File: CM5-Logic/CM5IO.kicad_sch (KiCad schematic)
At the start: 11 parts, among them J12 39291247, J2 B2B-PH-K-S, J20 ED555/4DS, J3 B2B-PH-K-S, J4 39291087, J6 691210910006, J7 691210910006

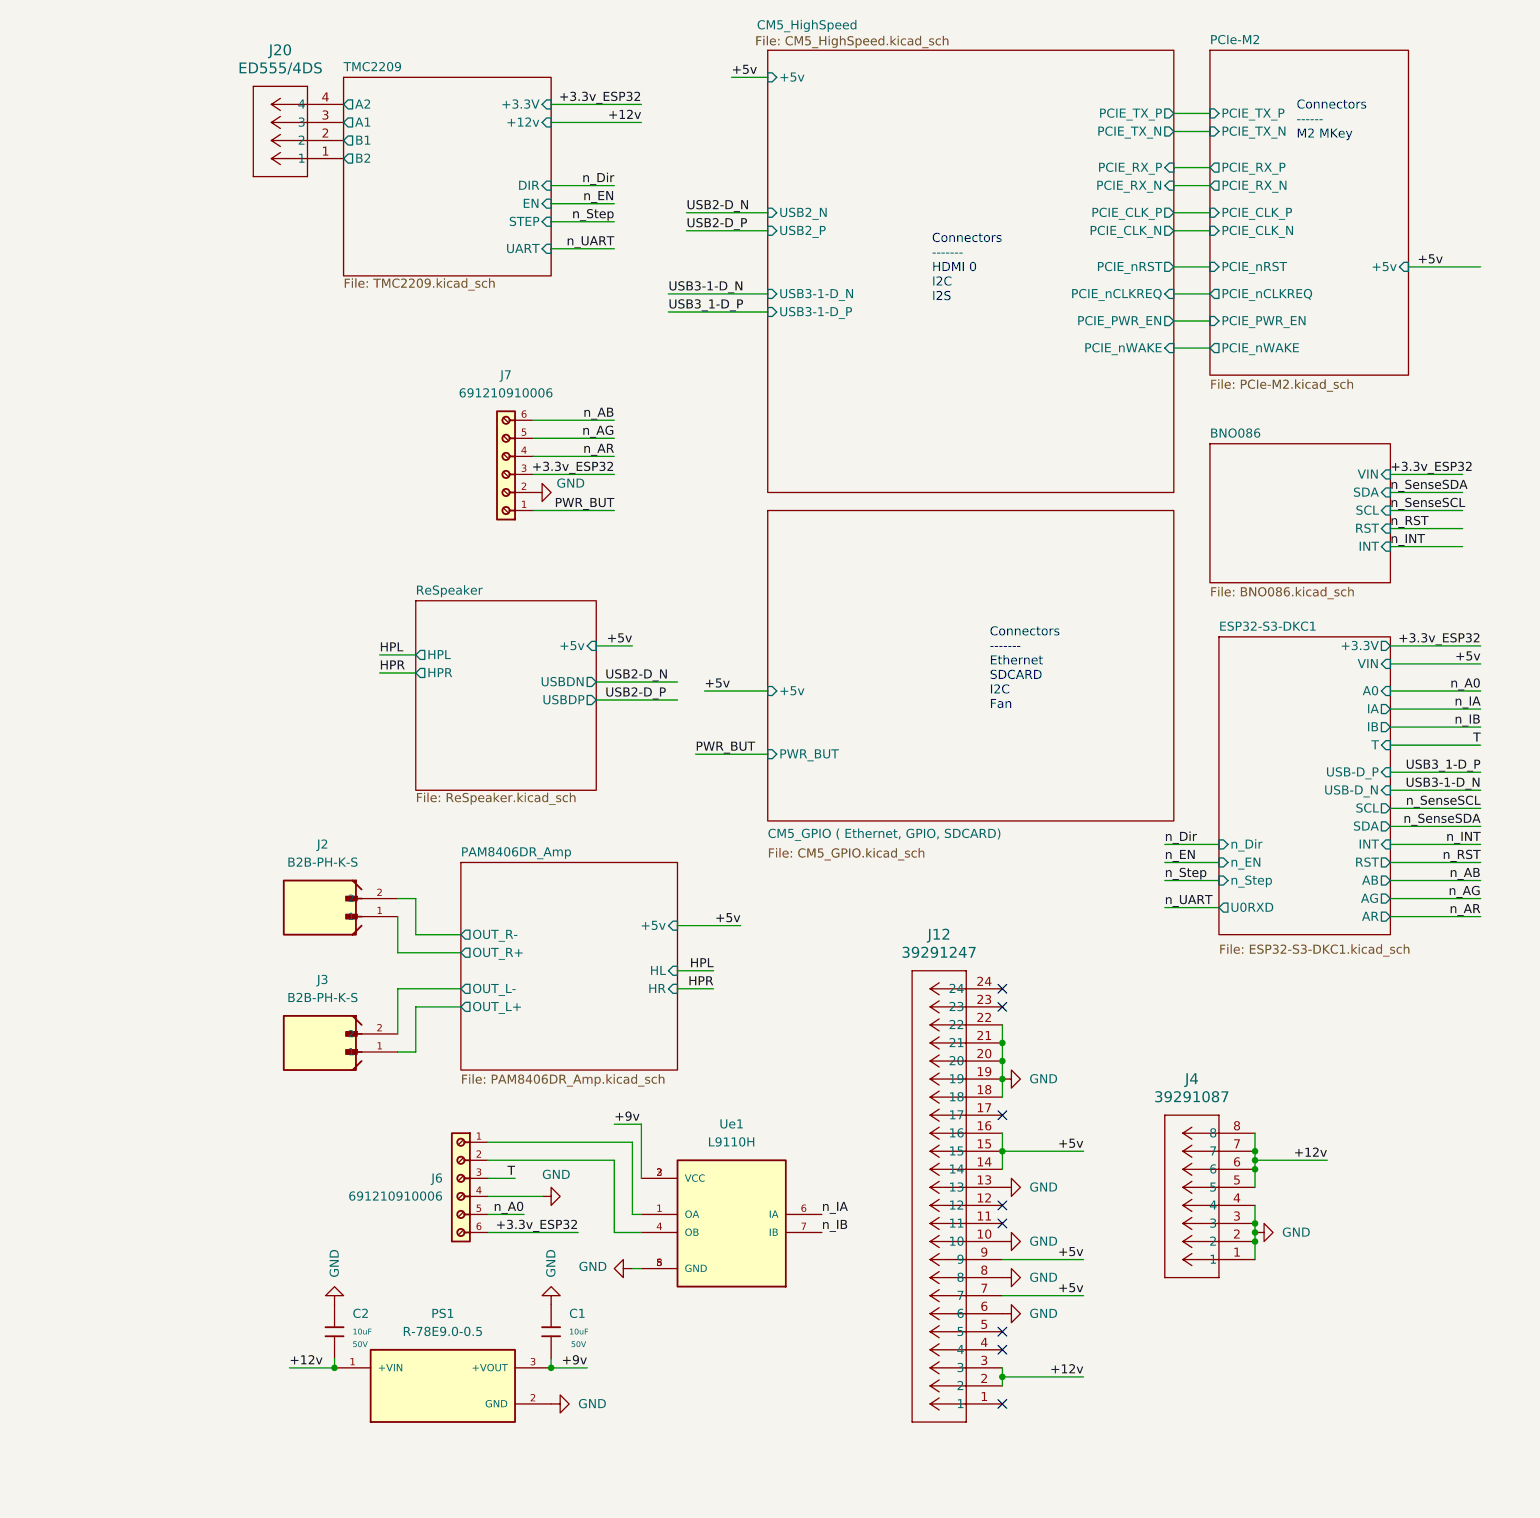
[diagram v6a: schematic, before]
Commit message: changes USB port, adds TMC2209 SilentStepStick footprint, redoes PCB Layout
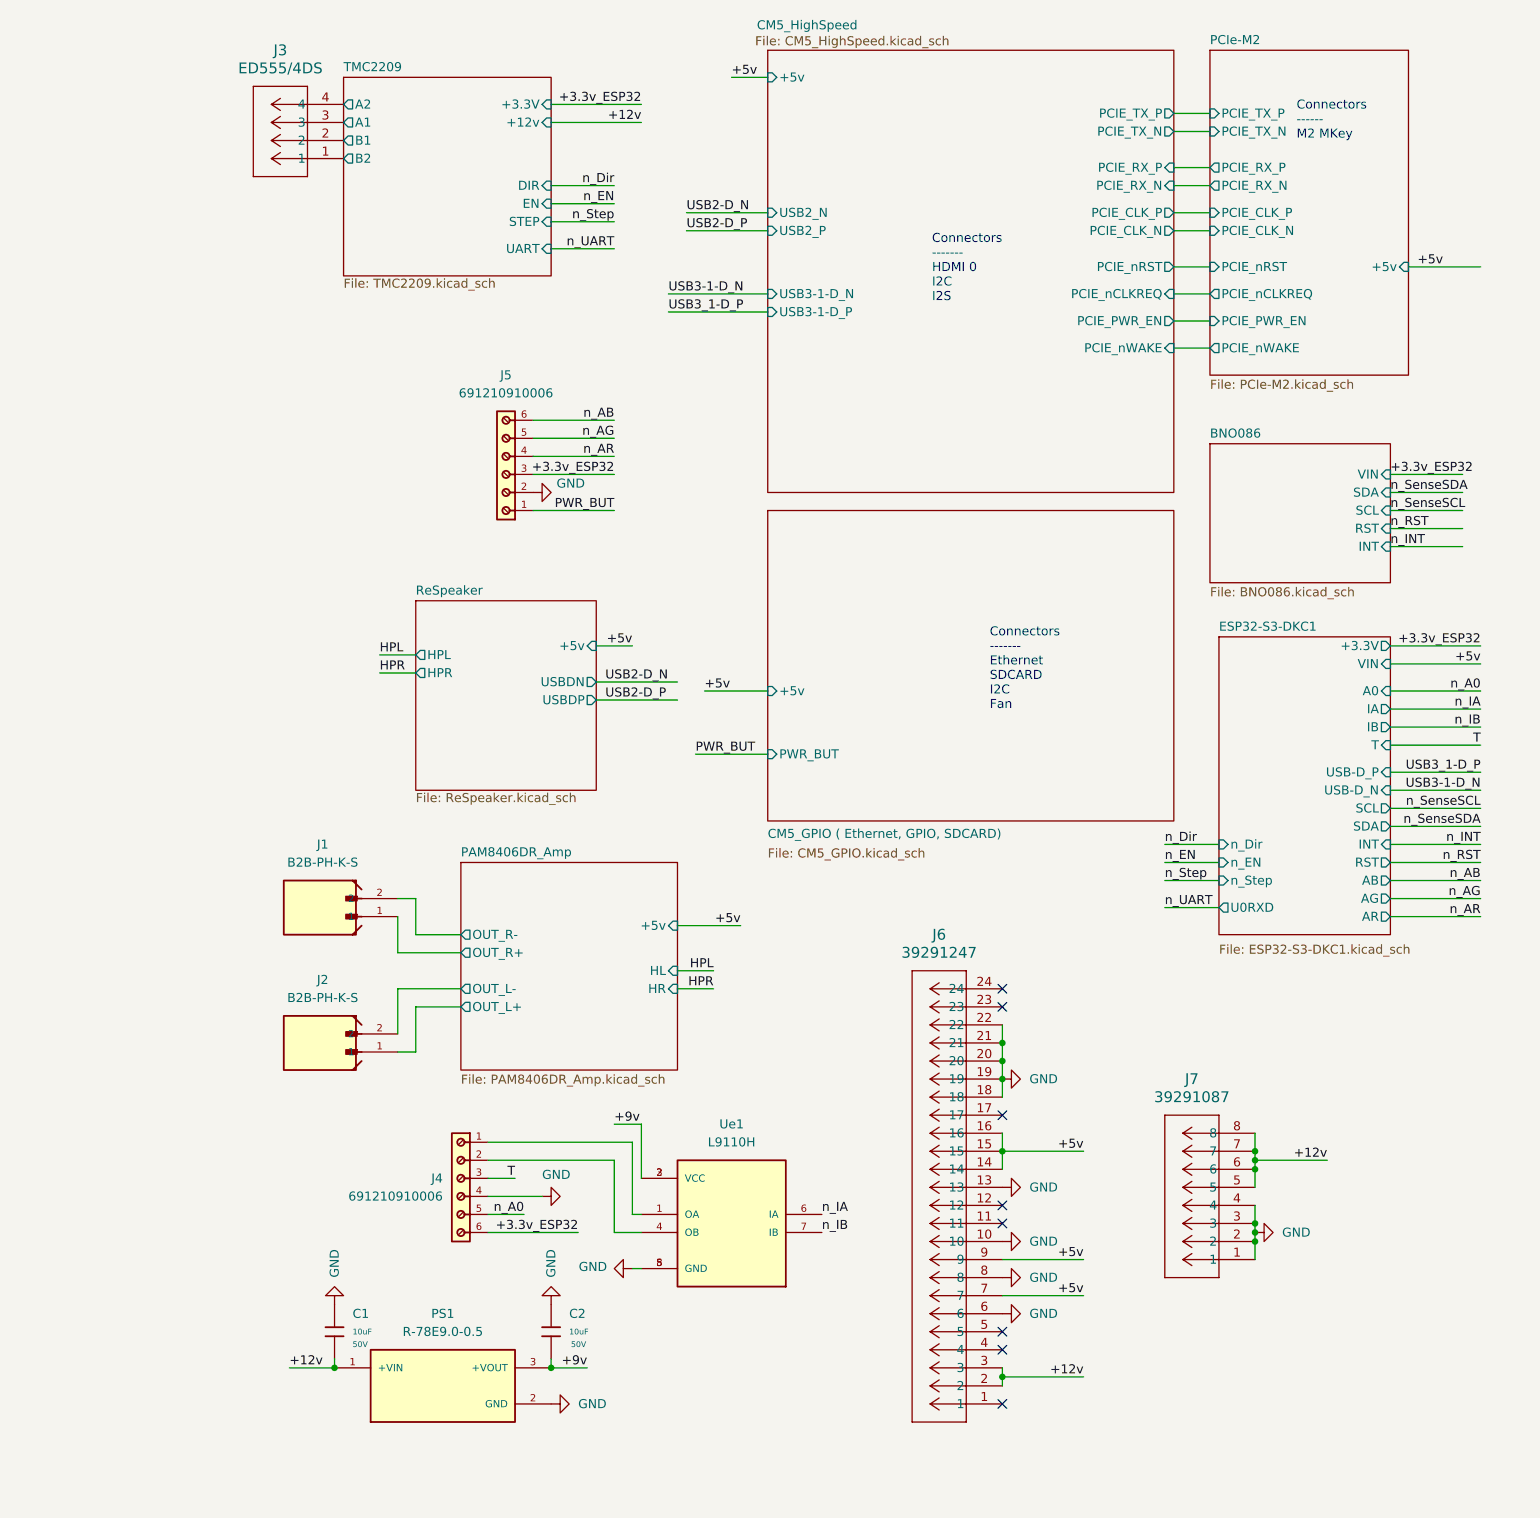
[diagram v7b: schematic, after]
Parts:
- PS1: footprint R-78E9.0-0.5:CONV_R-78E9.0-0.5 -> Custom Components:CONV_R-78E9.0-0.5
- renumbered C2 to C1, C1 to C2, J2 to J1, J3 to J2, J20 to J3, J6 to J4, J7 to J5, J12 to J6, J4 to J7
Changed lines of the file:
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@@
 		(dnp no)
 		(fields_autoplaced yes)
-		(property "Reference" "J4"
+		(property "Reference" "J7"
 			(at 509.27 179.07 0)
 			(effects
@@
 			(project ""
 				(path "/e63e39d7-6ac0-4ffd-8aa3-1841a4541b55"
-					(reference "J4")
+					(reference "J7")
 					(unit 1)
 				)
@@
 		(dnp no)
 		(fields_autoplaced yes)
-		(property "Reference" "#PWR074"
+		(property "Reference" "#PWR012"
 			(at 524.51 200.66 0)
 			(effects
@@
 			(project "CM5IO"
 				(path "/e63e39d7-6ac0-4ffd-8aa3-1841a4541b55"
-					(reference "#PWR074")
+					(reference "#PWR012")
 					(unit 1)
 				)
@@
 		(dnp no)
 		(fields_autoplaced yes)
-		(property "Reference" "J2"
+		(property "Reference" "J1"
 			(at 386.9531 146.05 0)
 			(effects
@@
 			(project "CM5IO"
 				(path "/e63e39d7-6ac0-4ffd-8aa3-1841a4541b55"
-					(reference "J2")
+					(reference "J1")
 					(unit 1)
 				)
@@
 		(on_board yes)
 		(dnp no)
-		(property "Reference" "#PWR06"
+		(property "Reference" "#PWR03"
 			(at 424.18 195.58 0)
 			(effects
@@
 			(project "CM5IO"
 				(path "/e63e39d7-6ac0-4ffd-8aa3-1841a4541b55"
-					(reference "#PWR06")
+					(reference "#PWR03")
 					(unit 1)
 				)
@@
 		(on_board yes)
 		(dnp no)
-		(property "Reference" "#PWR01"
+		(property "Reference" "#PWR04"
 			(at 419.1 204.47 0)
 			(effects
@@
 			(project "CM5IO"
 				(path "/e63e39d7-6ac0-4ffd-8aa3-1841a4541b55"
-					(reference "#PWR01")
+					(reference "#PWR04")
 					(unit 1)
 				)
@@
 		(dnp no)
 		(fields_autoplaced yes)
-		(property "Reference" "#PWR066"
+		(property "Reference" "#PWR08"
 			(at 488.95 194.31 0)
 			(effects
@@
 			(project ""
 				(path "/e63e39d7-6ac0-4ffd-8aa3-1841a4541b55"
-					(reference "#PWR066")
+					(reference "#PWR08")
 					(unit 1)
 				)
@@
 		(dnp no)
 		(fields_autoplaced yes)
-		(property "Reference" "#PWR073"
+		(property "Reference" "#PWR09"
 			(at 488.95 201.93 0)
 			(effects
@@
 			(project "CM5IO"
 				(path "/e63e39d7-6ac0-4ffd-8aa3-1841a4541b55"
-					(reference "#PWR073")
+					(reference "#PWR09")
 					(unit 1)
 				)
@@
 		(dnp no)
 		(fields_autoplaced yes)
-		(property "Reference" "#PWR072"
+		(property "Reference" "#PWR010"
 			(at 488.95 207.01 0)
 			(effects
@@
 			(project "CM5IO"
 				(path "/e63e39d7-6ac0-4ffd-8aa3-1841a4541b55"
-					(reference "#PWR072")
+					(reference "#PWR010")
 					(unit 1)
 				)
@@
 		(dnp no)
 		(fields_autoplaced yes)
-		(property "Reference" "J7"
+		(property "Reference" "J5"
 			(at 412.75 80.01 90)
 			(effects
@@
 			(project ""
 				(path "/e63e39d7-6ac0-4ffd-8aa3-1841a4541b55"
-					(reference "J7")
+					(reference "J5")
 					(unit 1)
 				)
@@
 		(dnp no)
 		(fields_autoplaced yes)
-		(property "Reference" "#PWR067"
+		(property "Reference" "#PWR07"
 			(at 488.95 179.07 0)
 			(effects
@@
 			(project "CM5IO"
 				(path "/e63e39d7-6ac0-4ffd-8aa3-1841a4541b55"
-					(reference "#PWR067")
+					(reference "#PWR07")
 					(unit 1)
 				)
@@
 		(dnp no)
 		(fields_autoplaced yes)
-		(property "Reference" "J3"
+		(property "Reference" "J2"
 			(at 386.9531 165.1 0)
 			(effects
@@
 			(project "CM5IO"
 				(path "/e63e39d7-6ac0-4ffd-8aa3-1841a4541b55"
-					(reference "J3")
+					(reference "J2")
 					(unit 1)
 				)
@@
 		(on_board yes)
 		(dnp no)
-		(property "Reference" "#PWR08"
+		(property "Reference" "#PWR02"
 			(at 422.91 96.52 0)
 			(effects
@@
 			(project ""
 				(path "/e63e39d7-6ac0-4ffd-8aa3-1841a4541b55"
-					(reference "#PWR08")
+					(reference "#PWR02")
 					(unit 1)
 				)
@@
 		(on_board yes)
 		(dnp no)
-		(property "Reference" "C1"
+		(property "Reference" "C2"
 			(at 421.64 212.0899 0)
 			(effects
@@
 			(project "CM5IO"
 				(path "/e63e39d7-6ac0-4ffd-8aa3-1841a4541b55"
-					(reference "C1")
+					(reference "C2")
 					(unit 1)
 				)
@@
 		(dnp no)
 		(fields_autoplaced yes)
-		(property "Reference" "J6"
+		(property "Reference" "J4"
 			(at 403.86 193.0399 90)
 			(effects
@@
 			(project ""
 				(path "/e63e39d7-6ac0-4ffd-8aa3-1841a4541b55"
-					(reference "J6")
+					(reference "J4")
 					(unit 1)
 				)
@@
 		(dnp no)
 		(fields_autoplaced yes)
-		(property "Reference" "J20"
+		(property "Reference" "J3"
 			(at 381 34.29 0)
 			(effects
@@
 			(project ""
 				(path "/e63e39d7-6ac0-4ffd-8aa3-1841a4541b55"
-					(reference "J20")
+					(reference "J3")
 					(unit 1)
 				)
@@
 		(on_board yes)
 		(dnp no)
-		(property "Reference" "#PWR04"
+		(property "Reference" "#PWR06"
 			(at 424.18 205.74 0)
 			(effects
@@
 			(project "CM5IO"
 				(path "/e63e39d7-6ac0-4ffd-8aa3-1841a4541b55"
-					(reference "#PWR04")
+					(reference "#PWR06")
 					(unit 1)
 				)
@@
 		(dnp no)
 		(fields_autoplaced yes)
-		(property "Reference" "J12"
+		(property "Reference" "J6"
 			(at 473.71 158.75 0)
 			(effects
@@
 			(project ""
 				(path "/e63e39d7-6ac0-4ffd-8aa3-1841a4541b55"
-					(reference "J12")
+					(reference "J6")
 					(unit 1)
 				)
@@
 		(on_board yes)
 		(dnp no)
-		(property "Reference" "#PWR02"
+		(property "Reference" "#PWR01"
 			(at 388.62 204.47 0)
 			(effects
@@
 			(project "CM5IO"
 				(path "/e63e39d7-6ac0-4ffd-8aa3-1841a4541b55"
-					(reference "#PWR02")
+					(reference "#PWR01")
 					(unit 1)
 				)
@@
 		(on_board yes)
 		(dnp no)
-		(property "Reference" "#PWR03"
+		(property "Reference" "#PWR05"
 			(at 425.45 224.79 0)
 			(effects
@@
 			(project "CM5IO"
 				(path "/e63e39d7-6ac0-4ffd-8aa3-1841a4541b55"
-					(reference "#PWR03")
+					(reference "#PWR05")
 					(unit 1)
 				)
@@
 			)
 		)
-		(property "Footprint" "R-78E9.0-0.5:CONV_R-78E9.0-0.5"
+		(property "Footprint" "Custom Components:CONV_R-78E9.0-0.5"
 			(at 403.86 222.25 0)
 			(effects
@@
 		(dnp no)
 		(fields_autoplaced yes)
-		(property "Reference" "#PWR069"
+		(property "Reference" "#PWR011"
 			(at 488.95 212.09 0)
 			(effects
@@
 			(project "CM5IO"
 				(path "/e63e39d7-6ac0-4ffd-8aa3-1841a4541b55"
-					(reference "#PWR069")
+					(reference "#PWR011")
 					(unit 1)
 				)
@@
 		(on_board yes)
 		(dnp no)
-		(property "Reference" "C2"
+		(property "Reference" "C1"
 			(at 391.16 212.0899 0)
 			(effects
@@
 			(project "CM5IO"
 				(path "/e63e39d7-6ac0-4ffd-8aa3-1841a4541b55"
-					(reference "C2")
-					(unit 1)
-				)
+					(reference "C1")
+					(unit 1)
+				)

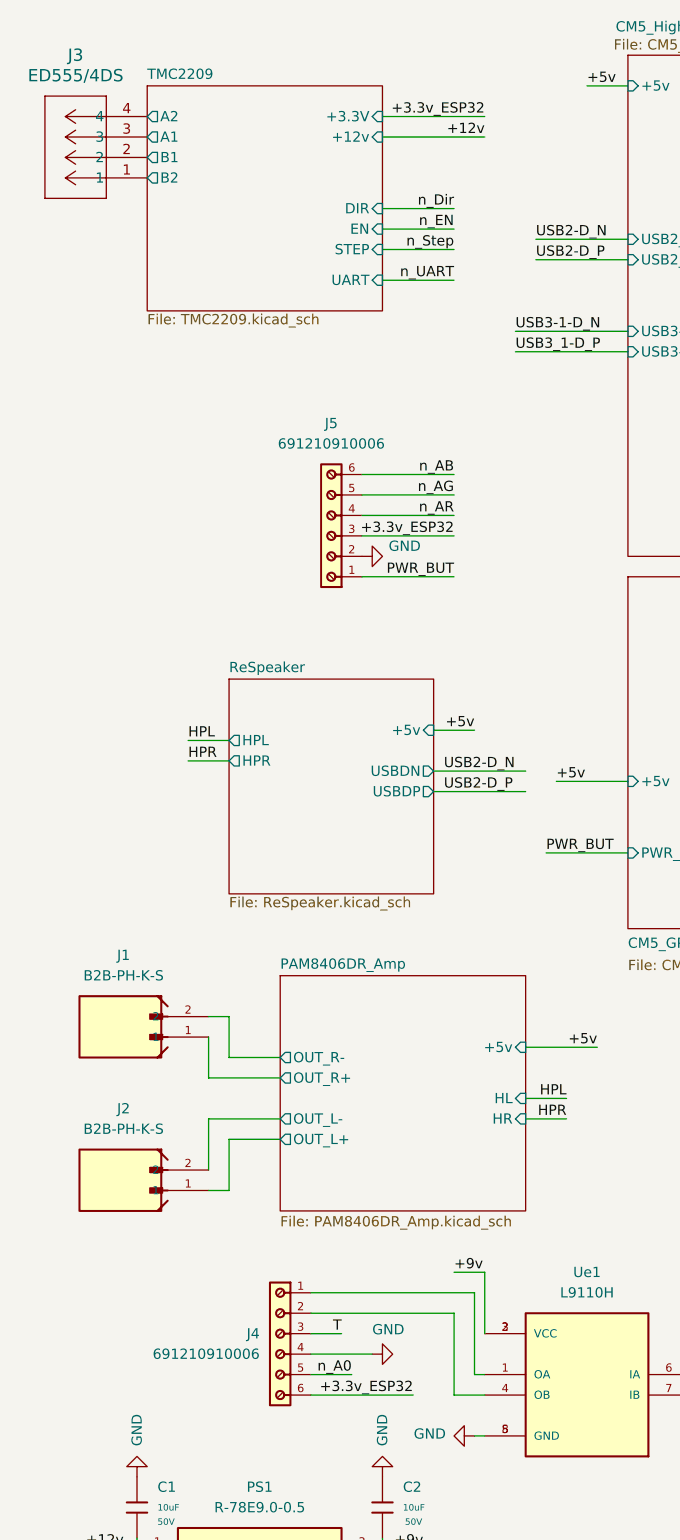
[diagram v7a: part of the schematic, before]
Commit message: Finishes PCB Pad Layout, Updates LED Status Circuit to RPI Foundations newest version
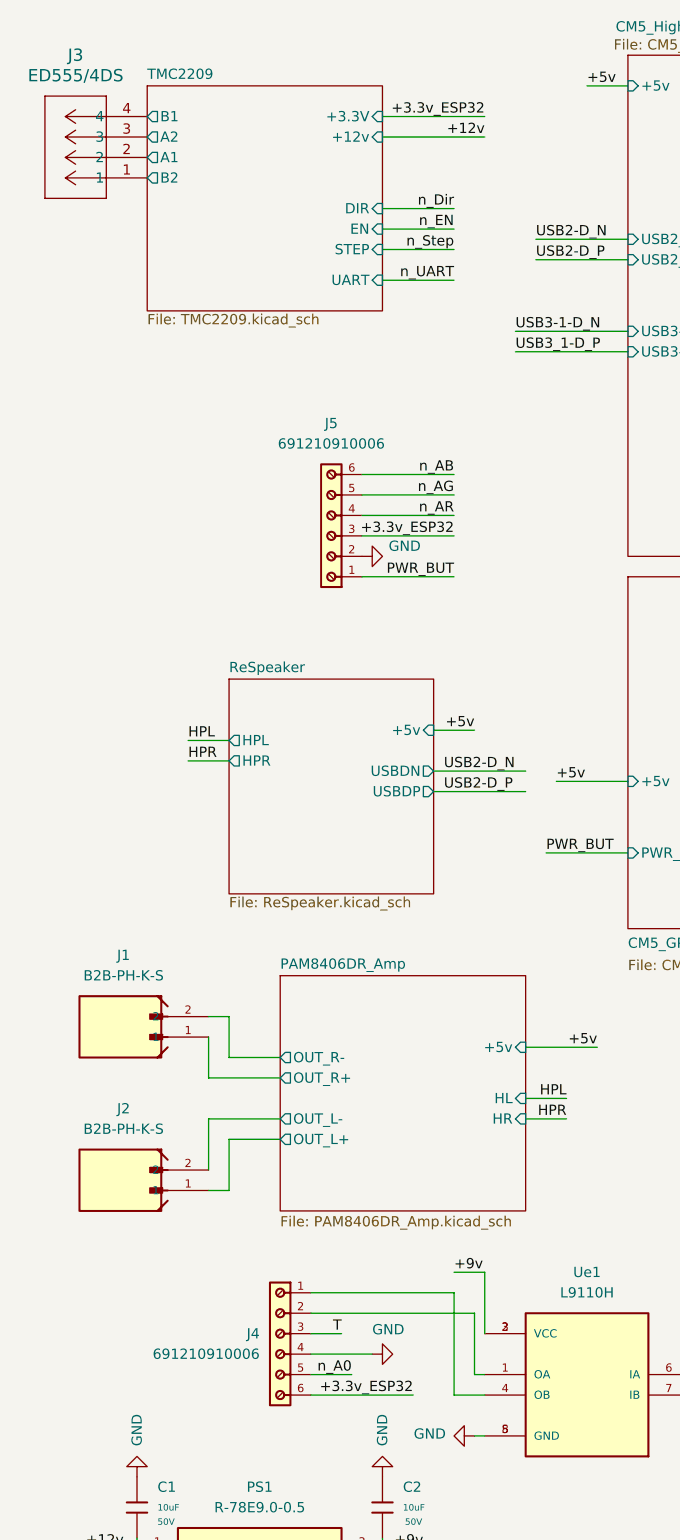
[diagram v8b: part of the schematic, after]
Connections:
- net TMC2209/A1: now also J3.2; no longer J3.3
- net TMC2209/A2: now also J3.3; no longer J3.4
- net TMC2209/B1: now also J3.4; no longer J3.2
- net at J4.1: now also Ue1.4 (OB); no longer Ue1.1 (OA)
- net at J4.2: now also Ue1.1 (OA); no longer Ue1.4 (OB)
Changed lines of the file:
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@@
 	(wire
 		(pts
-			(xy 410.21 187.96) (xy 430.53 187.96)
-		)
-		(stroke
-			(width 0)
-			(type default)
-		)
-	)
-	(wire
-		(pts
 			(xy 406.4 168.91) (xy 400.05 168.91)
 		)
@@
 	(wire
 		(pts
-			(xy 410.21 190.5) (xy 427.99 190.5)
-		)
-		(stroke
-			(width 0)
-			(type default)
-		)
-	)
-	(wire
-		(pts
 			(xy 482.6 220.98) (xy 482.6 222.25)
 		)
@@
 	(wire
 		(pts
-			(xy 430.53 187.96) (xy 430.53 198.12)
-		)
-		(stroke
-			(width 0)
-			(type default)
-		)
-	)
-	(wire
-		(pts
 			(xy 549.91 151.13) (xy 537.21 151.13)
 		)
@@
 	(wire
 		(pts
+			(xy 410.21 190.5) (xy 430.53 190.5)
+		)
+		(stroke
+			(width 0)
+			(type default)
+		)
+	)
+	(wire
+		(pts
 			(xy 482.6 173.99) (xy 482.6 176.53)
 		)
@@
 	(wire
 		(pts
+			(xy 427.99 187.96) (xy 410.21 187.96)
+		)
+		(stroke
+			(width 0)
+			(type default)
+		)
+	)
+	(wire
+		(pts
 			(xy 518.16 199.39) (xy 518.16 200.66)
 		)
@@
 	(wire
 		(pts
+			(xy 430.53 190.5) (xy 430.53 198.12)
+		)
+		(stroke
+			(width 0)
+			(type default)
+		)
+	)
+	(wire
+		(pts
 			(xy 537.21 96.52) (xy 547.37 96.52)
 		)
@@
 	(wire
 		(pts
-			(xy 427.99 190.5) (xy 427.99 200.66)
+			(xy 427.99 187.96) (xy 427.99 200.66)
 		)
 		(stroke
@@
 		)
 		(instances
-			(project ""
+			(project "CM5IO"
 				(path "/e63e39d7-6ac0-4ffd-8aa3-1841a4541b55"
 					(reference "J3")
@@
 		)
 		(pin "A1" output
-			(at 389.89 44.45 180)
+			(at 389.89 46.99 180)
 			(effects
 				(font
@@
 		)
 		(pin "A2" output
-			(at 389.89 41.91 180)
+			(at 389.89 44.45 180)
 			(effects
 				(font
@@
 		)
 		(pin "B1" output
-			(at 389.89 46.99 180)
+			(at 389.89 41.91 180)
 			(effects
 				(font
